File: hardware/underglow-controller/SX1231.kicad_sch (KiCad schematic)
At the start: 32 parts, among them U501 SX1231HIMLTRT, U502 PE42421SCAA-Z, Y501 32mhz

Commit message: Bom fillout + wiring
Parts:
- C514, C518: MPN (none) -> 04025A5R6BAT2A
- C515, C517: MPN (none) -> 04023C103KAT2A
- C519: MPN (none) -> 500R07S1R2BV4T
- C521: MPN (none) -> 250R05L0R5AV4T
- L505: MPN (none) -> MLJ1005WR12JT000
- R501: MPN (none) -> RMCF0402JT10K0
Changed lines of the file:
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@@
       (effects (font (size 1.27 1.27)) hide)
     )
-    (property "MPN" "" (id 5) (at 80.01 161.925 0)
+    (property "MPN" "MLJ1005WR12JT000" (id 5) (at 80.01 161.925 0)
       (effects (font (size 1.27 1.27)) hide)
     )
@@
       (effects (font (size 1.27 1.27)) hide)
     )
-    (property "Description" "" (id 4) (at 95.25 161.925 0)
-      (effects (font (size 1.27 1.27)) hide)
-    )
-    (property "MPN" "" (id 5) (at 95.25 161.925 0)
+    (property "Description" "CAP CER 5.6PF 50V NP0 0402" (id 4) (at 95.25 161.925 0)
+      (effects (font (size 1.27 1.27)) hide)
+    )
+    (property "MPN" "04025A5R6BAT2A" (id 5) (at 95.25 161.925 0)
       (effects (font (size 1.27 1.27)) hide)
     )
@@
       (effects (font (size 1.27 1.27)) hide)
     )
-    (property "Description" "" (id 4) (at 163.195 144.145 0)
-      (effects (font (size 1.27 1.27)) hide)
-    )
-    (property "MPN" "" (id 5) (at 163.195 144.145 0)
+    (property "Description" "CAP CER 0.5PF 25V C0G/NP0 0201" (id 4) (at 163.195 144.145 0)
+      (effects (font (size 1.27 1.27)) hide)
+    )
+    (property "MPN" "250R05L0R5AV4T" (id 5) (at 163.195 144.145 0)
       (effects (font (size 1.27 1.27)) hide)
     )
@@
       (effects (font (size 1.27 1.27)) hide)
     )
-    (property "Description" "" (id 4) (at 151.765 160.655 0)
-      (effects (font (size 1.27 1.27)) hide)
-    )
-    (property "MPN" "" (id 5) (at 151.765 160.655 0)
+    (property "Description" "RES 10K OHM 5% 1/16W 0402" (id 4) (at 151.765 160.655 0)
+      (effects (font (size 1.27 1.27)) hide)
+    )
+    (property "MPN" "RMCF0402JT10K0" (id 5) (at 151.765 160.655 0)
       (effects (font (size 1.27 1.27)) hide)
     )
@@
       (effects (font (size 1.27 1.27)) hide)
     )
-    (property "Description" "" (id 4) (at 99.695 137.795 0)
-      (effects (font (size 1.27 1.27)) hide)
-    )
-    (property "MPN" "" (id 5) (at 99.695 137.795 0)
+    (property "Description" "CAP CER 5.6PF 50V NP0 0402" (id 4) (at 99.695 137.795 0)
+      (effects (font (size 1.27 1.27)) hide)
+    )
+    (property "MPN" "04025A5R6BAT2A" (id 5) (at 99.695 137.795 0)
       (effects (font (size 1.27 1.27)) hide)
     )
@@
       (effects (font (size 1.27 1.27)) hide)
     )
-    (property "Description" "" (id 4) (at 111.125 158.115 0)
-      (effects (font (size 1.27 1.27)) hide)
-    )
-    (property "MPN" "" (id 5) (at 111.125 158.115 0)
+    (property "Description" "CAP CER 10000PF 25V X7R 0402" (id 4) (at 111.125 158.115 0)
+      (effects (font (size 1.27 1.27)) hide)
+    )
+    (property "MPN" "04023C103KAT2A" (id 5) (at 111.125 158.115 0)
       (effects (font (size 1.27 1.27)) hide)
     )
@@
       (effects (font (size 1.27 1.27)) hide)
     )
-    (property "Description" "" (id 4) (at 149.225 146.685 0)
-      (effects (font (size 1.27 1.27)) hide)
-    )
-    (property "MPN" "" (id 5) (at 149.225 146.685 0)
+    (property "Description" "CAP CER 1.2PF 50V C0G/NP0 0402" (id 4) (at 149.225 146.685 0)
+      (effects (font (size 1.27 1.27)) hide)
+    )
+    (property "MPN" "500R07S1R2BV4T" (id 5) (at 149.225 146.685 0)
       (effects (font (size 1.27 1.27)) hide)
     )
@@
       (effects (font (size 1.27 1.27)) hide)
     )
-    (property "Description" "" (id 4) (at 111.125 153.035 0)
-      (effects (font (size 1.27 1.27)) hide)
-    )
-    (property "MPN" "" (id 5) (at 111.125 153.035 0)
-      (effects (font (size 1.27 1.27)) hide)
-    )
+    (property "Description" "CAP CER 10000PF 25V X7R 0402" (id 4) (at 111.125 153.035 0)
+      (effects (font (size 1.27 1.27)) hide)
+    )
+    (property "MPN" "04023C103KAT2A" (id 5) (at 111.125 153.035 0)
+      (effects (font (size 1.27 1.27)) hide)
+    )

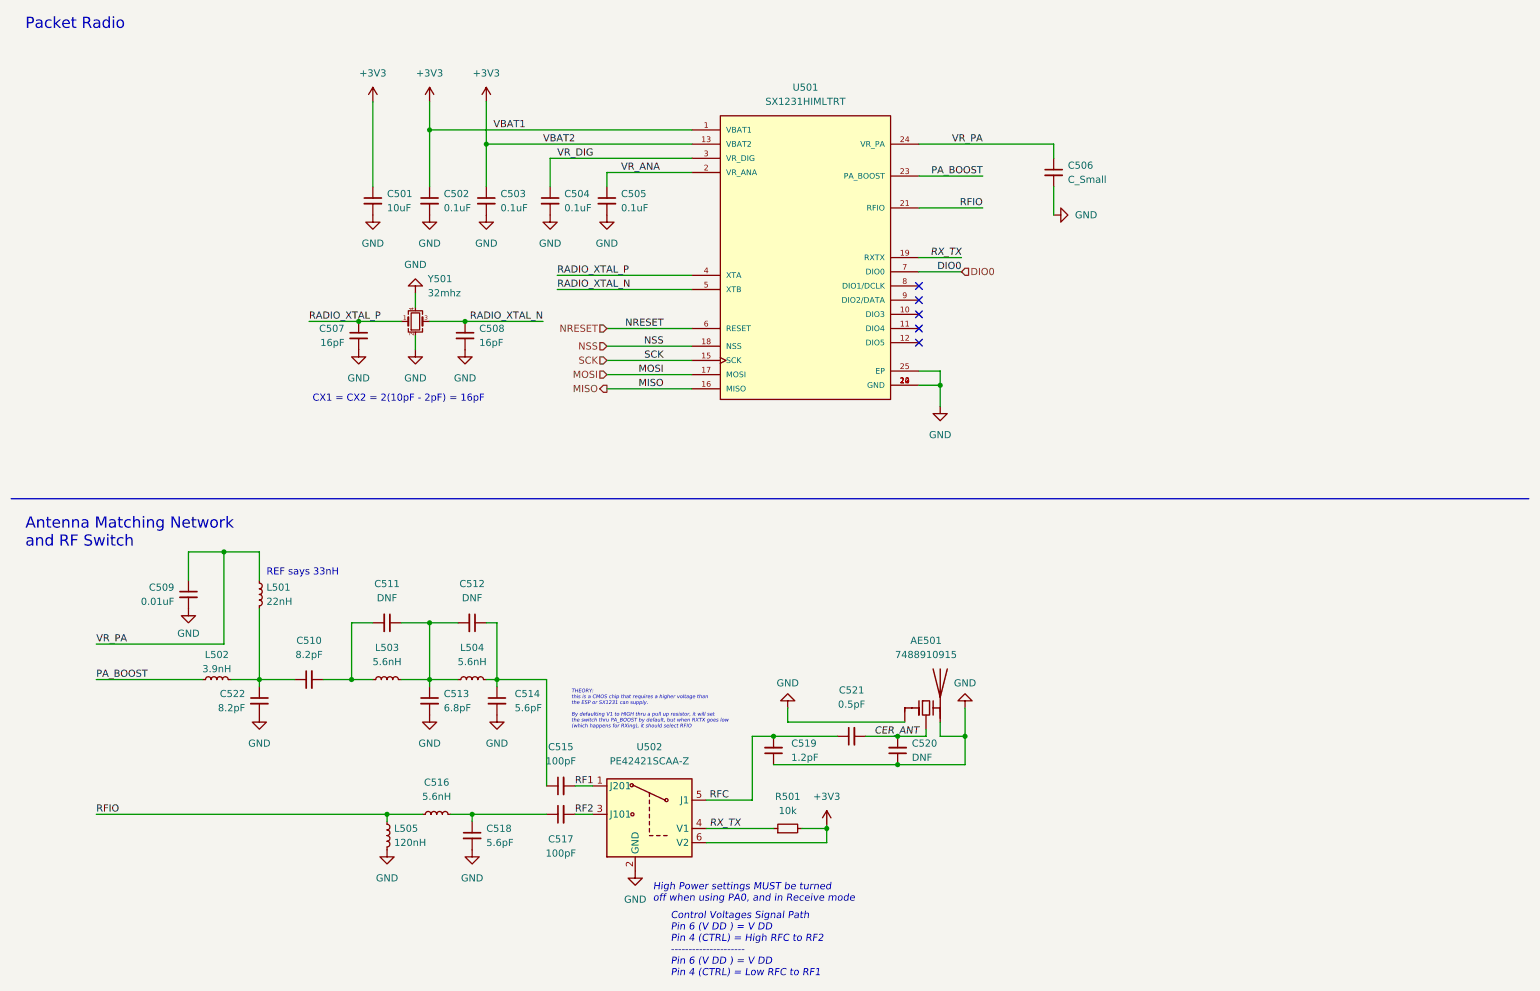
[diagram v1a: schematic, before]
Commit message: hw updates based on prototype issues
* Removes unused hardware and firmware projectes
* Adds some documentation and bom
* cleanup READMEs
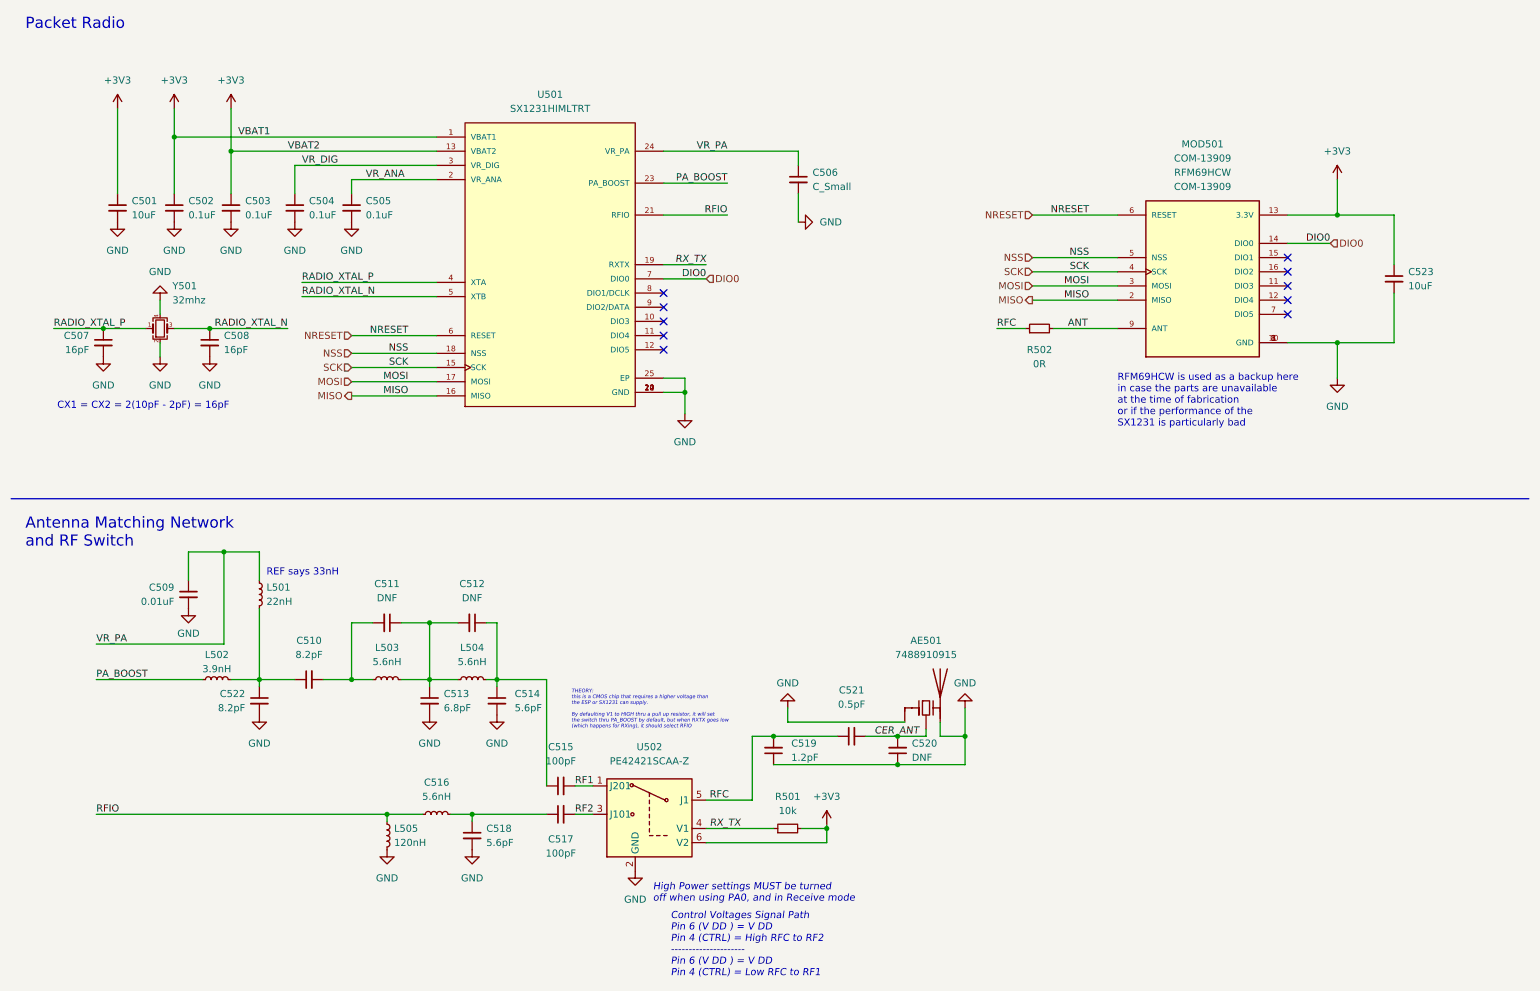
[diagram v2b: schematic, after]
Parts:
- added C523: 10uF, Capacitor_SMD:C_0805_2012Metric, symbol Device:C_Small
- added MOD501: COM-13909, RF_Module:HOPERF_RFM9XW_SMD, symbol ConeCodes:COM-13909
- added R502: 0R, Resistor_SMD:R_0402_1005Metric, symbol Device:R_Small
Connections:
- net +3V3: now also C523.1, MOD501.13 (3.3V)
- net DIO0: now also MOD501.14 (DIO0)
- net GND: now also C523.2, MOD501.1 (GND), MOD501.10 (GND), MOD501.8 (GND)
- net MISO: now also MOD501.2 (MISO)
- net MOSI: now also MOD501.3 (MOSI)
- net NRESET: now also MOD501.6 (RESET)
- net NSS: now also MOD501.5 (NSS)
- net RFC: now also R502.1
- net SCK: now also MOD501.4 (SCK)
- new net ANT: MOD501.9 (ANT), R502.2
- no-connect marks 5 -> 10
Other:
- note added: "RFM69HCW is used as a backup here in case the parts are unavailable at the time of fabrication or if the performance of the SX1231 is particularly bad"
- company: cone.codes -> Connor Rigby
- title: CAN RGB Controller V5 -> ${Title}
- moved on the sheet: C501, C502, C503, C504, C505, C506, C507, C508, U501, Y501

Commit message: hw updates based on latest boards
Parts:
- added J501: U.FL-R-SMT-1(10), HRS_U.FL-R-SMT-1(10), symbol ConeCodes:U.FL-R-SMT-1(10)
- added R503, R504: 0R, Resistor_SMD:R_0402_1005Metric, symbol Device:R_Small
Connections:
- net ANT: now also R504.2
- net GND: now also J501.1, J501.3
- net RFC: now also R503.1
- new net U.FL: J501.2, R503.2, R504.1
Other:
- moved on the sheet: AE501, C509, C510, C511, C512, C513, C514, C515, C516, C517, C518, C519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

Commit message: https://www.youtube.com/watch?v=FZUcpVmEHuk&ab_channel=billwurtz
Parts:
- C509: MPN C0402C103M5RECAUTO -> HMK105B7103MVHFE
- C510, C522: MPN 04025A8R2DAT2A -> 04023A8R2BAT2A
- C515, C517: MPN 04023C103KAT2A -> CGA2B2NP01H101J050BA
- C521: MPN 250R05L0R5AV4T -> C0402C508D3GAC7867
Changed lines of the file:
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@@
       (effects (font (size 1.27 1.27)) hide)
     )
-    (property "MPN" "04025A8R2DAT2A" (id 5) (at 57.15 138.43 0)
+    (property "MPN" "04023A8R2BAT2A" (id 5) (at 57.15 138.43 0)
       (effects (font (size 1.27 1.27)) hide)
     )
@@
       (effects (font (size 1.27 1.27)) hide)
     )
-    (property "MPN" "250R05L0R5AV4T" (id 5) (at 163.83 144.78 0)
+    (property "MPN" "C0402C508D3GAC7867" (id 5) (at 163.83 144.78 0)
       (effects (font (size 1.27 1.27)) hide)
     )
@@
       (effects (font (size 1.27 1.27)) hide)
     )
-    (property "MPN" "04025A8R2DAT2A" (id 5) (at 66.04 134.62 0)
+    (property "MPN" "04023A8R2BAT2A" (id 5) (at 66.04 134.62 0)
       (effects (font (size 1.27 1.27)) hide)
     )
@@
       (effects (font (size 1.27 1.27)) hide)
     )
-    (property "MPN" "C0402C103M5RECAUTO" (id 5) (at 44.45 119.38 0)
+    (property "MPN" "HMK105B7103MVHFE" (id 5) (at 44.45 119.38 0)
       (effects (font (size 1.27 1.27)) hide)
     )
@@
       (effects (font (size 1.27 1.27)) hide)
     )
-    (property "MPN" "04023C103KAT2A" (id 5) (at 111.76 158.75 0)
+    (property "MPN" "CGA2B2NP01H101J050BA" (id 5) (at 111.76 158.75 0)
       (effects (font (size 1.27 1.27)) hide)
     )
@@
       (effects (font (size 1.27 1.27)) hide)
     )
-    (property "MPN" "04023C103KAT2A" (id 5) (at 111.76 153.67 0)
-      (effects (font (size 1.27 1.27)) hide)
-    )
+    (property "MPN" "CGA2B2NP01H101J050BA" (id 5) (at 111.76 153.67 0)
+      (effects (font (size 1.27 1.27)) hide)
+    )

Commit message: hardware updates
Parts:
- removed C501: 10uF, Capacitor_SMD:C_0805_2012Metric, symbol Device:C_Small
- removed C502, C503, C504, C505: 0.1uF, Capacitor_SMD:C_0402_1005Metric, symbol Device:C_Small
- removed C506: C_Small, Capacitor_SMD:C_0402_1005Metric, symbol Device:C_Small
- removed C507, C508: 16pF, Capacitor_SMD:C_0402_1005Metric, symbol Device:C_Small
- removed C509: 0.01uF, Capacitor_SMD:C_0402_1005Metric, symbol Device:C_Small
- removed C510, C522: 8.2pF, Capacitor_SMD:C_0402_1005Metric, symbol Device:C_Small
- removed C511, C512: DNF, Capacitor_SMD:C_0402_1005Metric, symbol Device:C_Small
- removed C513: 6.8pF, Capacitor_SMD:C_0402_1005Metric, symbol Device:C_Small
- removed C514, C518: 5.6pF, Capacitor_SMD:C_0402_1005Metric, symbol Device:C_Small
- removed C515, C517: 100pF, Capacitor_SMD:C_0402_1005Metric, symbol Device:C_Small
- removed C516, L503, L504: 5.6nH, Inductor_SMD:L_0402_1005Metric, symbol Device:L_Small
- removed C519: 1.2pF, Capacitor_SMD:C_0402_1005Metric, symbol Device:C_Small
- removed L501: 22nH, Inductor_SMD:L_0402_1005Metric, symbol Device:L_Small
- removed L502: 3.9nH, Inductor_SMD:L_0402_1005Metric, symbol Device:L_Small
- removed L505: 120nH, Inductor_SMD:L_0402_1005Metric, symbol Device:L_Small
- removed R501: 10k, Resistor_SMD:R_0402_1005Metric, symbol Device:R_Small
- removed U501: SX1231HIMLTRT, Package_DFN_QFN:QFN-24-1EP_5x5mm_P0.65mm_EP3.4x3.4mm_ThermalVias, symbol ConeCodes:SX1231HIMLTRT
- removed U502: PE42421SCAA-Z, Package_TO_SOT_SMD:SOT-363_SC-70-6, symbol RF_Switch:AS179-92LF
- removed Y501: 32mhz, Crystal:Crystal_SMD_2520-4Pin_2.5x2.0mm, symbol Device:Crystal_GND24_Small
- J501: footprint HRS_U.FL-R-SMT-1(10) -> ConeCodes:HRS_U.FL-R-SMT-1(10)
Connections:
- net RFC: no longer C521.1, R503.1
- net U.FL: no longer R503.2
- no-connect marks 10 -> 5
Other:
- note removed: "Antenna Matching Network and RF Switch"
- note removed: "CX1 = CX2 = 2(10pF - 2pF) = 16pF"
- note removed: "Control Voltages Signal Path Pin 6 (V DD ) = V DD Pin 4 (CTRL) = High RFC to RF2 --------------------- Pin 6 (V DD ) = V DD Pin 4 (CTRL) = Low RFC to RF1"
- note removed: "High Power settings MUST be turned off when using PA0, and in Receive mode"
- note removed: "REF says 33nH"
- note removed: "RFM69HCW is used as a backup here in case the parts are unavailable at the time of fabrication or if the performance of the SX1231 is particularly bad"
- note removed: "THEORY: this is a CMOS chip that requires a higher voltage than the ESP or SX1231 can supply. By defaulting V1 to HIGH thru a pull up resistor, it will set the switch thru PA_BOOST by default, but when RXTX goes low (which happens for RXing), it should select RFIO"
- moved on the sheet: AE501, C520, C521, C523, J501, MOD501, R502, R503, R504

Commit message: ughughughugh
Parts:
- removed R503: 0R, Resistor_SMD:R_0402_1005Metric, symbol Device:R_Small
- added C501: 0.5pF, Capacitor_SMD:C_0402_1005Metric, symbol Device:C_Small
- added C502: DNF, Capacitor_SMD:C_0402_1005Metric, symbol Device:C_Small
- added L501, L502: 2nH, Inductor_SMD:L_0402_1005Metric, symbol Device:L_Small
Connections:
- net RFC is gone; now on net CER_ANT: R502.1
- net CER_ANT: now also L501.1; no longer AE501.3 (FEED), C520.2
- net GND: now also C521.1, C501.1, C502.1
- net U.FL: no longer names the net of J501.2
- net U.FL: now also C502.2, L502.2; no longer R504.1
- new net: AE501.3 (FEED), C520.2, L501.2
- new net U.FL_ANT: C501.2, L502.1, R504.1
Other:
- moved on the sheet: AE501, C520, C521, J501

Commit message: hw updates pt 69 thousand
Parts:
- removed L501, L502: 2nH, Inductor_SMD:L_0402_1005Metric, symbol Device:L_Small
- added C503: 0.5pF, Capacitor_SMD:C_0402_1005Metric, symbol Device:C_Small
- added C504: DNF, Capacitor_SMD:C_0402_1005Metric, symbol Device:C_Small
- added TP501: NSS, TestPoint:TestPoint_Pad_D1.0mm, symbol Connector:TestPoint
- added TP502: SCK, TestPoint:TestPoint_Pad_D1.0mm, symbol Connector:TestPoint
- added TP503: MOSI, TestPoint:TestPoint_Pad_D1.0mm, symbol Connector:TestPoint
- added TP504: MISO, TestPoint:TestPoint_Pad_D1.0mm, symbol Connector:TestPoint
- added TP506: DIO0, TestPoint:TestPoint_Pad_D1.0mm, symbol Connector:TestPoint
- AE501: MPN (none) -> 7488910915
- C501, C521: value 0.5pF -> DNF; MPN C0402C508D3GAC7867 -> (none)
- C520: value DNF -> 1.2pF; MPN (none) -> C0402C129D3GAC7867
- MOD501: MPN RFM69HCW -> COM-13909
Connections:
- net CER_ANT: now also C503.2
- net DIO0: now also TP506.1
- net MISO: now also TP504.1
- net MOSI: now also TP503.1
- net NSS: now also TP501.1
- net SCK: now also TP502.1
- net U.FL_ANT: now also C504.2
- net at C502.2, J501.2: now also C504.1
- net at AE501.3 (FEED), C520.2: now also C503.1

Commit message: hardware: prepare for production run
Signed-off-by: Connor Rigby <connorr@hey.com>
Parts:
- MOD501: MANUFACTURER SparkFun Electronics -> (none)
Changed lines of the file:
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@@
       (effects (font (size 1.27 1.27)) (justify left bottom) hide)
     )
-    (property "MANUFACTURER" "SparkFun Electronics" (id 4) (at 57.15 52.07 0)
+    (property "MANUFACTURER" "" (id 4) (at 57.15 52.07 0)
       (effects (font (size 1.27 1.27)) (justify left bottom) hide)
     )
